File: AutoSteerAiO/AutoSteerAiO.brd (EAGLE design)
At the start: 114.3 x 99.1 mm, 84 parts, among them J4 CONNECTOR 1x5 PINS, K4 CB1A-P-12V, U1 VX7805-1000

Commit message: Add files via upload
added led autosteer
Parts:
- added LED3: LED, adafruit:LED5MM
- added R21: 1k, resistor:0207/7
- added T1: BC547, transistor:TO92
- D5: device SparkFun-Connectors:1X02 -> SparkFun-Connectors:1X01
- R20: value 1k -> 5k7
- moved D5 3.13 mm to (102.9, 62.5)
- turned R20 to 0 degrees
- renumbered R15 to R20
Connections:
- removed net D5.: D5.1, R20.1
- new net N$23: R20.2, T1.2
- new net N$24: LED3.A, R21.1
- new net N$27: LED3.K, T1.3
- net +5V: now also R21.2
- net D5: now also D5.1, R20.1; no longer R20.2
- net GND: now also T1.1; no longer D5.2
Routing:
- net GND: track 586.4 -> 550.0 mm
- net N$23: track 0.00 -> 34.7 mm
- net +5V: track 245.5 -> 268.1 mm
- net D5: track 87.4 -> 106.7 mm
- net D5.: track 12.9 -> 0.00 mm
- net N$27: track 0.00 -> 7.94 mm
- net N$24: track 0.00 -> 7.12 mm
- net N$25: track 58.5 -> 61.2 mm

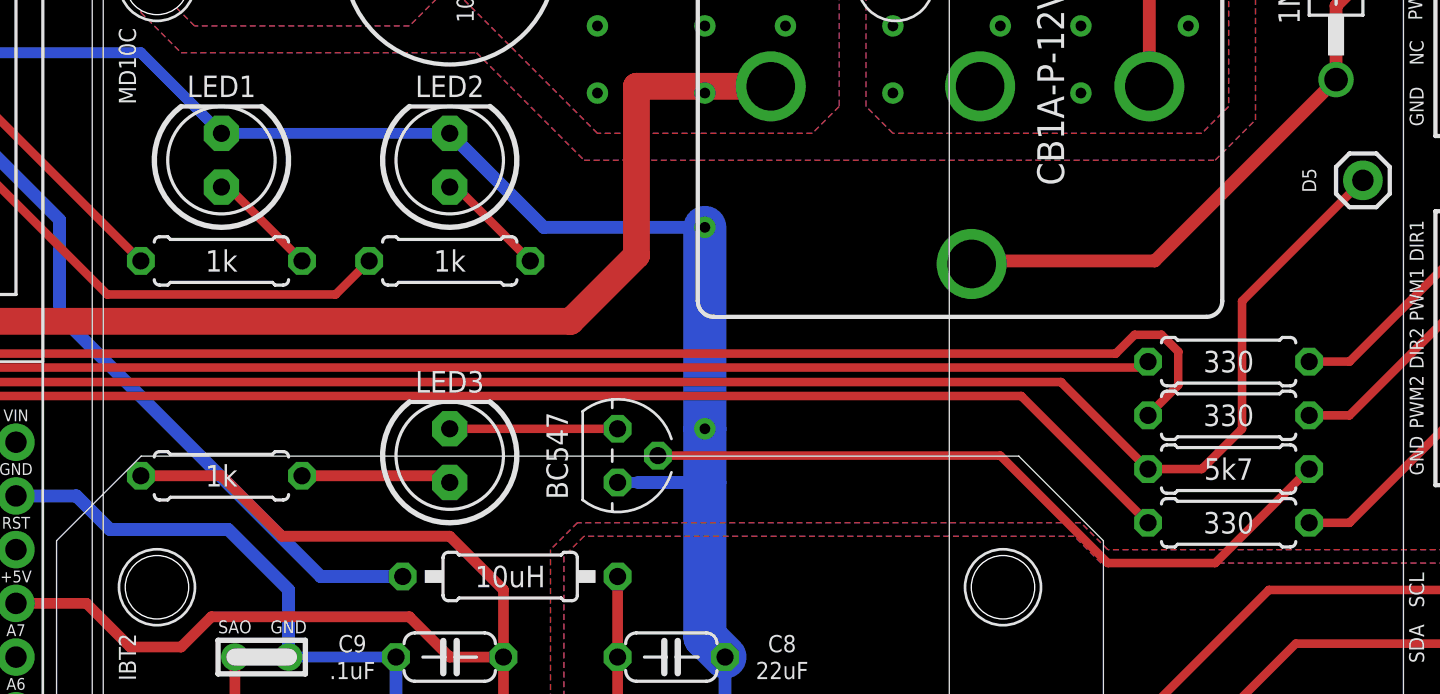
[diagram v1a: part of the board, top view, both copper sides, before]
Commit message: Add files via upload
added led autosteer
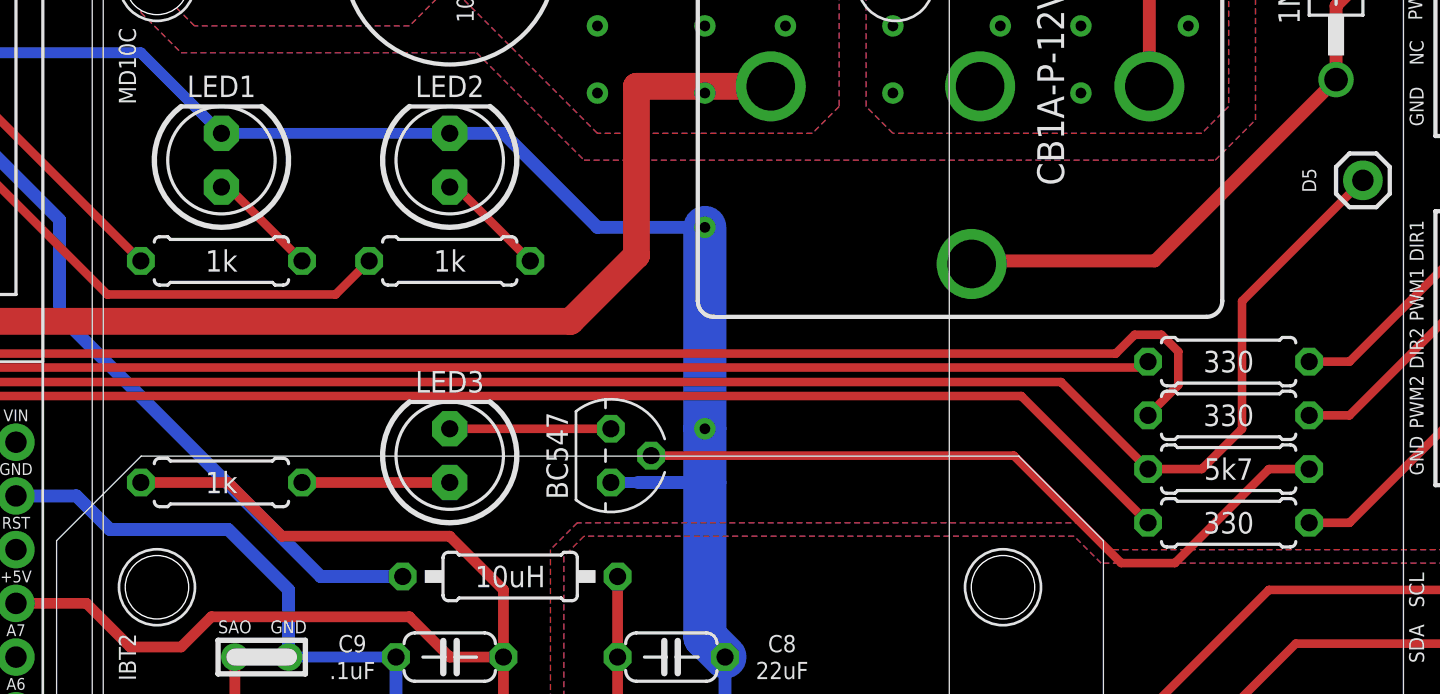
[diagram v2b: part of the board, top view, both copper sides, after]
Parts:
- moved R21 0.32 mm to (48.9, 48.3)
- moved T1 0.32 mm to (67.3, 49.5)
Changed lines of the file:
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@@
 <attribute name="CYTRON-PC" value="CN-2600PS-05" x="109.855" y="49.53" size="1.778" layer="27" rot="R90" display="off"/>
 <attribute name="DESC" value="2600 PCB Connector" x="109.855" y="49.53" size="1.778" layer="27" rot="R90" display="off"/>
+<attribute name="LABEL" value="" x="112.776" y="48.133" size="0.762" layer="21" font="vector" ratio="15" rot="R90" align="top-left"/>
 <attribute name="LABEL" value="" x="112.776" y="48.133" size="0.762" layer="51" font="vector" ratio="15" rot="R90" align="top-left"/>
-<attribute name="LABEL" value="" x="112.776" y="48.133" size="0.762" layer="21" font="vector" ratio="15" rot="R90" align="top-left"/>
 <attribute name="LABEL" value="" x="109.855" y="49.53" size="1.778" layer="27" rot="R90" display="off"/>
 <attribute name="MF" value="" x="109.855" y="49.53" size="1.778" layer="27" rot="R90" display="off"/>
@@
 </element>
 <element name="U$13" library="#MMA8542Q" package="MMA8542Q" value="MMA8542Q" x="43.18" y="8.255" smashed="yes"/>
-<element name="T1" library="transistor" library_urn="urn:adsk.eagle:library:402" package="TO92" package3d_urn="urn:adsk.eagle:package:28523/2" value="BC547" x="67.6275" y="49.53" smashed="yes" rot="R270">
+<element name="T1" library="transistor" library_urn="urn:adsk.eagle:library:402" package="TO92" package3d_urn="urn:adsk.eagle:package:28523/2" value="BC547" x="67.31" y="49.53" smashed="yes" rot="R270">
 <attribute name="VALUE" x="64.77" y="49.53" size="1.016" layer="25" font="vector" ratio="14" rot="R270" align="center"/>
 </element>
@@
 <attribute name="VALUE" x="96.52" y="48.895" size="1.016" layer="25" font="vector" ratio="12" align="center"/>
 </element>
-<element name="R21" library="resistor" library_urn="urn:adsk.eagle:library:348" package="0207/7" package3d_urn="urn:adsk.eagle:package:23493/2" value="1k" x="48.895" y="48.5775" smashed="yes" rot="R180">
-<attribute name="MF" value="" x="48.895" y="48.5775" size="1.778" layer="27" rot="R180" display="off"/>
-<attribute name="MPN" value="" x="48.895" y="48.5775" size="1.778" layer="27" rot="R180" display="off"/>
-<attribute name="OC_NEWARK" value="unknown" x="48.895" y="48.5775" size="1.778" layer="27" rot="R180" display="off"/>
-<attribute name="VALUE" x="48.895" y="48.5775" size="1.016" layer="25" font="vector" ratio="12" align="center"/>
+<element name="R21" library="resistor" library_urn="urn:adsk.eagle:library:348" package="0207/7" package3d_urn="urn:adsk.eagle:package:23493/2" value="1k" x="48.895" y="48.26" smashed="yes" rot="R180">
+<attribute name="MF" value="" x="48.895" y="48.26" size="1.778" layer="27" rot="R180" display="off"/>
+<attribute name="MPN" value="" x="48.895" y="48.26" size="1.778" layer="27" rot="R180" display="off"/>
+<attribute name="OC_NEWARK" value="unknown" x="48.895" y="48.26" size="1.778" layer="27" rot="R180" display="off"/>
+<attribute name="VALUE" x="48.895" y="48.26" size="1.016" layer="25" font="vector" ratio="12" align="center"/>
 </element>
 <element name="LED3" library="adafruit" library_urn="urn:adsk.eagle:library:420" package="LED5MM" package3d_urn="urn:adsk.eagle:package:6240538/1" value="LED" x="59.69" y="49.53" smashed="yes" rot="R90">
@@
 <wire x1="62.23" y1="40.005" x2="62.23" y2="43.18" width="0.508" layer="1"/>
 <wire x1="62.23" y1="43.18" x2="59.69" y2="45.72" width="0.508" layer="1"/>
-<wire x1="51.7525" y1="45.72" x2="48.895" y2="48.5775" width="0.508" layer="1"/>
-<wire x1="48.895" y1="48.5775" x2="45.085" y2="48.5775" width="0.508" layer="1"/>
+<wire x1="51.7525" y1="45.72" x2="49.2125" y2="48.26" width="0.508" layer="1"/>
+<wire x1="49.2125" y1="48.26" x2="45.085" y2="48.26" width="0.508" layer="1"/>
 <wire x1="59.69" y1="45.72" x2="51.7525" y2="45.72" width="0.508" layer="1"/>
 </signal>
@@
 <wire x1="109.855" y1="86.36" x2="98.425" y2="86.36" width="0.6096" layer="16"/>
 <wire x1="98.425" y1="86.36" x2="97.155" y2="85.09" width="0.6096" layer="16"/>
-<wire x1="71.755" y1="60.325" x2="64.135" y2="60.325" width="0.6096" layer="16"/>
-<wire x1="64.135" y1="60.325" x2="59.69" y2="64.77" width="0.6096" layer="16"/>
+<wire x1="71.755" y1="60.325" x2="66.675" y2="60.325" width="0.6096" layer="16"/>
+<wire x1="66.675" y1="60.325" x2="62.23" y2="64.77" width="0.6096" layer="16"/>
+<wire x1="62.23" y1="64.77" x2="59.69" y2="64.77" width="0.6096" layer="16"/>
 <wire x1="112.395" y1="66.04" x2="112.395" y2="49.53" width="0.6096" layer="16"/>
 <wire x1="112.395" y1="49.53" x2="109.855" y2="49.53" width="0.6096" layer="16"/>
@@
 <wire x1="57.15" y1="36.83" x2="57.15" y2="22.225" width="0.6096" layer="16"/>
 <contactref element="T1" pad="1"/>
-<wire x1="67.6275" y1="48.26" x2="68.58" y2="48.26" width="0.508" layer="16"/>
+<wire x1="67.31" y1="48.26" x2="68.58" y2="48.26" width="0.508" layer="16"/>
 <wire x1="68.58" y1="48.26" x2="69.215" y2="48.26" width="0.508" layer="16"/>
 <wire x1="71.755" y1="50.8" x2="71.755" y2="48.26" width="2.032" layer="16"/>
@@
 <contactref element="T1" pad="2"/>
 <contactref element="R20" pad="2"/>
-<wire x1="100.33" y1="48.895" x2="95.885" y2="44.45" width="0.4064" layer="1"/>
-<wire x1="90.805" y1="44.45" x2="85.725" y2="49.53" width="0.4064" layer="1"/>
-<wire x1="85.725" y1="49.53" x2="69.5325" y2="49.53" width="0.4064" layer="1"/>
-<wire x1="95.885" y1="44.45" x2="90.805" y2="44.45" width="0.4064" layer="1"/>
+<wire x1="100.33" y1="48.895" x2="98.425" y2="48.895" width="0.4064" layer="1"/>
+<wire x1="98.425" y1="48.895" x2="93.98" y2="44.45" width="0.4064" layer="1"/>
+<wire x1="91.44" y1="44.45" x2="86.36" y2="49.53" width="0.4064" layer="1"/>
+<wire x1="86.36" y1="49.53" x2="69.215" y2="49.53" width="0.4064" layer="1"/>
+<wire x1="93.98" y1="44.45" x2="91.44" y2="44.45" width="0.4064" layer="1"/>
 </signal>
 <signal name="N$24">
 <contactref element="LED3" pad="A"/>
 <contactref element="R21" pad="1"/>
-<wire x1="52.705" y1="48.5775" x2="59.3725" y2="48.5775" width="0.508" layer="1"/>
-<wire x1="59.3725" y1="48.5775" x2="59.69" y2="48.26" width="0.508" layer="1"/>
+<wire x1="52.705" y1="48.26" x2="59.69" y2="48.26" width="0.508" layer="1"/>
 </signal>
 <signal name="N$27">
 <contactref element="T1" pad="3"/>
 <contactref element="LED3" pad="K"/>
-<wire x1="67.6275" y1="50.8" x2="59.69" y2="50.8" width="0.4064" layer="1"/>
+<wire x1="67.31" y1="50.8" x2="59.69" y2="50.8" width="0.4064" layer="1"/>
 </signal>
 </signals>

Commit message: Add files via upload
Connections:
- net N$25: now also R16.1
- net N$26: no longer R16.1
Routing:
- net N$25: track 61.2 -> 94.8 mm
- net N$26: track 78.1 -> 57.7 mm
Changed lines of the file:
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@@
 <drawing>
 <settings>
-<setting alwaysvectorfont="no"/>
+<setting alwaysvectorfont="yes"/>
 <setting keepoldvectorfont="yes"/>
 <setting verticaltext="up"/>
@@
 <wire x1="3.7465" y1="9.779" x2="2.54" y2="10.9855" width="0.6096" layer="1"/>
 <wire x1="7.3025" y1="53.975" x2="2.54" y2="49.2125" width="0.6096" layer="1"/>
-<wire x1="43.4975" y1="57.15" x2="34.6075" y2="66.04" width="0.4064" layer="1"/>
-<wire x1="34.6075" y1="66.04" x2="11.43" y2="66.04" width="0.4064" layer="1"/>
+<wire x1="43.4975" y1="57.15" x2="34.925" y2="65.7225" width="0.4064" layer="1"/>
+<wire x1="34.925" y1="65.7225" x2="11.7475" y2="65.7225" width="0.4064" layer="1"/>
 <wire x1="54.2925" y1="57.15" x2="55.88" y2="58.7375" width="0.4064" layer="1"/>
 <wire x1="43.4975" y1="57.15" x2="54.2925" y2="57.15" width="0.4064" layer="1"/>
@@
 <wire x1="5.08" y1="66.5607" x2="5.08" y2="64.77" width="0.8128" layer="1"/>
 <wire x1="8.7122" y1="68.6054" x2="8.8646" y2="68.6054" width="0.4064" layer="1"/>
-<wire x1="8.8646" y1="68.6054" x2="11.43" y2="66.04" width="0.4064" layer="1"/>
+<wire x1="8.8646" y1="68.6054" x2="11.7475" y2="65.7225" width="0.4064" layer="1"/>
 <contactref element="C9" pad="2"/>
 <wire x1="62.23" y1="36.83" x2="62.23" y2="40.005" width="0.508" layer="1"/>
@@
 <contactref element="C3" pad="2"/>
 <contactref element="C5" pad="+"/>
-<contactref element="R16" pad="1"/>
 <contactref element="PS1" pad="1"/>
 <contactref element="C6" pad="2"/>
@@
 <wire x1="15.5575" y1="80.01" x2="15.555" y2="80.0125" width="0.8128" layer="1"/>
 <wire x1="15.555" y1="80.0125" x2="15.5525" y2="80.01" width="0.8128" layer="1"/>
-<wire x1="34.925" y1="74.93" x2="34.925" y2="68.8975" width="0.4064" layer="1"/>
-<wire x1="45.085" y1="58.7375" x2="34.925" y2="68.8975" width="0.4064" layer="1"/>
 <wire x1="15.5575" y1="90.5275" x2="15.5575" y2="86.36" width="0.8128" layer="1"/>
 <contactref element="U1" pad="1"/>
@@
 <wire x1="41.24075" y1="60.67675" x2="41.24075" y2="56.16325" width="0.6096" layer="16"/>
 <wire x1="19.40175" y1="64.73575" x2="37.18175" y2="64.73575" width="0.6096" layer="16"/>
+<contactref element="R16" pad="1"/>
+<wire x1="45.085" y1="58.7375" x2="36.83" y2="66.9925" width="0.4064" layer="1"/>
+<wire x1="36.83" y1="66.9925" x2="17.145" y2="66.9925" width="0.4064" layer="1"/>
+<wire x1="17.145" y1="66.9925" x2="15.5525" y2="68.585" width="0.4064" layer="1"/>
 </signal>
 <signal name="N$3">

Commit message: Add files via upload
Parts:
- moved D5 0.32 mm to (102.9, 62.9)
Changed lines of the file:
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@@
 <attribute name="OC_NEWARK" value="unknown" x="43.18" y="24.13" size="1.778" layer="27" display="off"/>
 </element>
-<element name="D5" library="SparkFun-Connectors" library_urn="urn:adsk.eagle:library:513" package="1X01" package3d_urn="urn:adsk.eagle:package:38028/1" value="CONNECTOR 1x1 PIN" x="102.87" y="62.5475" smashed="yes" rot="R90">
-<attribute name="MF" value="" x="102.87" y="62.5475" size="1.778" layer="27" rot="R90" display="off"/>
-<attribute name="MPN" value="" x="102.87" y="62.5475" size="1.778" layer="27" rot="R90" display="off"/>
-<attribute name="NAME" x="100.33" y="62.5475" size="0.6604" layer="25" font="vector" ratio="15" rot="R270" align="center"/>
-<attribute name="OC_NEWARK" value="unknown" x="102.87" y="62.5475" size="1.778" layer="27" rot="R90" display="off"/>
+<element name="D5" library="SparkFun-Connectors" library_urn="urn:adsk.eagle:library:513" package="1X01" package3d_urn="urn:adsk.eagle:package:38028/1" value="CONNECTOR 1x1 PIN" x="102.87" y="62.865" smashed="yes" rot="R90">
+<attribute name="MF" value="" x="102.87" y="62.865" size="1.778" layer="27" rot="R90" display="off"/>
+<attribute name="MPN" value="" x="102.87" y="62.865" size="1.778" layer="27" rot="R90" display="off"/>
+<attribute name="NAME" x="100.33" y="62.865" size="0.6604" layer="25" font="vector" ratio="15" rot="R270" align="center"/>
+<attribute name="OC_NEWARK" value="unknown" x="102.87" y="62.865" size="1.778" layer="27" rot="R90" display="off"/>
 </element>
 <element name="0" library="SparkFun-Connectors" library_urn="urn:adsk.eagle:library:513" package="1X03" package3d_urn="urn:adsk.eagle:package:38063/1" value="CONNECTOR 1x2 PINS" x="61.595" y="4.445" smashed="yes">
@@
 <wire x1="88.5952" y1="53.0098" x2="92.71" y2="48.895" width="0.4064" layer="1"/>
 <contactref element="D5" pad="1"/>
-<wire x1="102.87" y1="62.5475" x2="97.155" y2="56.8325" width="0.4064" layer="1"/>
-<wire x1="97.155" y1="56.8325" x2="97.155" y2="50.8" width="0.4064" layer="1"/>
+<wire x1="102.87" y1="62.865" x2="97.155" y2="57.15" width="0.4064" layer="1"/>
+<wire x1="97.155" y1="57.15" x2="97.155" y2="50.8" width="0.4064" layer="1"/>
 <wire x1="92.71" y1="48.895" x2="95.25" y2="48.895" width="0.4064" layer="1"/>
 <wire x1="95.25" y1="48.895" x2="97.155" y2="50.8" width="0.4064" layer="1"/>
